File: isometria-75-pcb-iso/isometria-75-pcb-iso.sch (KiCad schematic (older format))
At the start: 32 parts, among them J101 USB, J102 SPI, J103 Conn_01x01_Male, Q101 AO3400A, SW101 RST, SW102 BOOT, U101 XC6206P332MR, U102 STM32F072CBTx

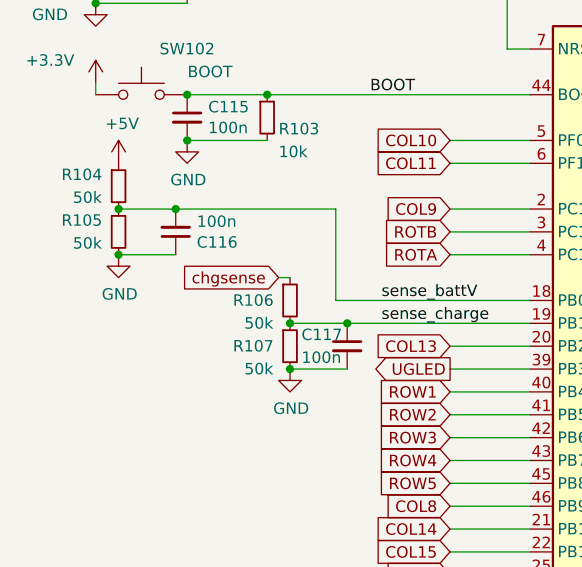
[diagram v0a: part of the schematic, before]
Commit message: final touches
changed some 0603 to 0402 for consistency, added vias to properly better ground planes, added LCSC part numbers for jlcpcb assembly
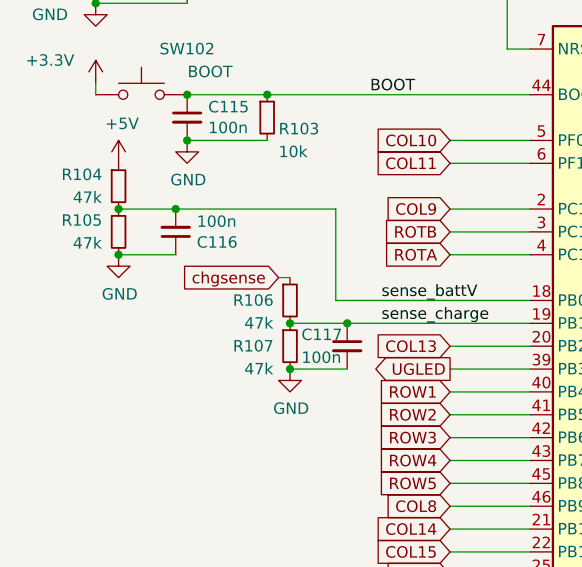
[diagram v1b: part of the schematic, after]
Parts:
- C101, C102: LCSC (none) -> C16133
- C103: LCSC (none) -> C7171
- C104, C106: footprint Capacitor_SMD:C_0603_1608Metric -> Capacitor_SMD:C_0402_1005Metric; LCSC (none) -> C52923
- C105, C112: footprint Capacitor_SMD:C_0603_1608Metric -> Capacitor_SMD:C_0402_1005Metric; LCSC (none) -> C23733
- C107, C108, C109, C110, C113, C114, C115, C116, C117: LCSC (none) -> C1525
- C111: LCSC (none) -> C23733
- J101, J102, J103: LCSC (none) -> /
- Q101: LCSC (none) -> C20917
- R101: LCSC (none) -> C25076
- R102: LCSC (none) -> C25077
- R103: LCSC (none) -> C25744
- R104, R105, R106, R107: value 50k -> 47k; LCSC (none) -> C25792
- SW101, SW102: LCSC (none) -> C318886
- U101: LCSC (none) -> C5446
- U102: LCSC (none) -> C81720
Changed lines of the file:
@@
 F 2 "Package_QFP:LQFP-48_7x7mm_P0.5mm" H 2850 3550 50  0001 R CNN
 F 3 "http://www.st.com/st-web-ui/static/active/en/resource/technical/document/datasheet/DM00090510.pdf" H 3450 4950 50  0001 C CNN
+F 4 "C81720" H 3450 4950 50  0001 C CNN "LCSC"
 	1    3450 4950
 	1    0    0    -1
@@
 F 2 "Capacitor_SMD:C_0402_1005Metric" H 4200 3550 50  0001 C CNN
 F 3 "~" H 4200 3550 50  0001 C CNN
+F 4 "C1525" H 4200 3550 50  0001 C CNN "LCSC"
 	1    4200 3550
 	1    0    0    -1
@@
 F 2 "Capacitor_SMD:C_0402_1005Metric" H 1250 3350 50  0001 C CNN
 F 3 "~" H 1250 3350 50  0001 C CNN
+F 4 "C1525" H 1250 3350 50  0001 C CNN "LCSC"
 	1    1250 3350
 	1    0    0    -1
@@
 F 2 "Resistor_SMD:R_0402_1005Metric" H 3750 3250 50  0001 C CNN
 F 3 "~" H 3750 3250 50  0001 C CNN
+F 4 "C25077" H 3750 3250 50  0001 C CNN "LCSC"
 	1    3750 3250
 	0    -1   -1   0
@@
 F 2 "Package_TO_SOT_SMD:SOT-23" H 4400 1450 50  0001 C CNN
 F 3 "https://datasheet.lcsc.com/szlcsc/Alpha-Omega-Semicon-AOS-AO3400A_C20917.pdf" H 4200 1350 50  0001 C CNN
+F 4 "C20917" H 4200 1350 50  0001 C CNN "LCSC"
 	1    4200 1350
 	1    0    0    -1
@@
 F 2 "Capacitor_SMD:C_0402_1005Metric" H 1950 4950 50  0001 C CNN
 F 3 "~" H 1950 4950 50  0001 C CNN
+F 4 "C1525" H 1950 4950 50  0001 C CNN "LCSC"
 	1    1950 4950
 	1    0    0    -1
@@
 P 1700 4950
 F 0 "R107" H 1450 4950 50  0000 L CNN
-F 1 "50k" H 1500 4850 50  0000 L CNN
+F 1 "47k" H 1500 4850 50  0000 L CNN
 F 2 "Resistor_SMD:R_0402_1005Metric" H 1700 4950 50  0001 C CNN
 F 3 "~" H 1700 4950 50  0001 C CNN
+F 4 "C25792" H 1700 4950 50  0001 C CNN "LCSC"
 	1    1700 4950
 	1    0    0    -1
@@
 P 1700 4750
 F 0 "R106" H 1450 4750 50  0000 L CNN
-F 1 "50k" H 1500 4650 50  0000 L CNN
+F 1 "47k" H 1500 4650 50  0000 L CNN
 F 2 "Resistor_SMD:R_0402_1005Metric" H 1700 4750 50  0001 C CNN
 F 3 "~" H 1700 4750 50  0001 C CNN
+F 4 "C25792" H 1700 4750 50  0001 C CNN "LCSC"
 	1    1700 4750
 	1    0    0    -1
@@
 F 2 "Resistor_SMD:R_0402_1005Metric" H 3900 1350 50  0001 C CNN
 F 3 "~" H 3900 1350 50  0001 C CNN
+F 4 "C25076" H 3900 1350 50  0001 C CNN "LCSC"
 	1    3900 1350
 	0    -1   1    0
@@
 F 2 "Connector_JST:JST_SH_SM05B-SRSS-TB_1x05-1MP_P1.00mm_Horizontal" H 950 1150 50  0001 C CNN
 F 3 "http://www.jst-mfg.com/product/pdf/eng/ePH.pdf" H 950 1150 50  0001 C CNN
+F 4 "/" H 950 1150 50  0001 C CNN "LCSC"
 	1    950  1150
 	-1   0    0    1
@@
 F 0 "C106" H 3292 2496 50  0000 L CNN
 F 1 "1u" H 3292 2405 50  0000 L CNN
-F 2 "Capacitor_SMD:C_0603_1608Metric" H 3200 2450 50  0001 C CNN
+F 2 "Capacitor_SMD:C_0402_1005Metric" H 3200 2450 50  0001 C CNN
 F 3 "~" H 3200 2450 50  0001 C CNN
+F 4 "C52923" H 3200 2450 50  0001 C CNN "LCSC"
 	1    3200 2450
 	1    0    0    -1
@@
 F 0 "C104" H 1942 2496 50  0000 L CNN
 F 1 "1u" H 1942 2405 50  0000 L CNN
-F 2 "Capacitor_SMD:C_0603_1608Metric" H 1850 2450 50  0001 C CNN
+F 2 "Capacitor_SMD:C_0402_1005Metric" H 1850 2450 50  0001 C CNN
 F 3 "~" H 1850 2450 50  0001 C CNN
+F 4 "C52923" H 1850 2450 50  0001 C CNN "LCSC"
 	1    1850 2450
 	1    0    0    -1
@@
 F 2 "Package_TO_SOT_SMD:SOT-23" H 2800 2525 50  0001 C CIN
 F 3 "https://www.torexsemi.com/file/xc6206/XC6206.pdf" H 2800 2300 50  0001 C CNN
+F 4 "C5446" H 2800 2300 50  0001 C CNN "LCSC"
 	1    2800 2300
 	1    0    0    -1
@@
 F 2 "Capacitor_SMD:C_0402_1005Metric" H 5200 2450 50  0001 C CNN
 F 3 "~" H 5200 2450 50  0001 C CNN
+F 4 "C23733" H 5200 2450 50  0001 C CNN "LCSC"
 	1    5200 2450
 	1    0    0    -1
@@
 F 2 "Capacitor_SMD:C_0402_1005Metric" H 4800 2450 50  0001 C CNN
 F 3 "~" H 4800 2450 50  0001 C CNN
+F 4 "C1525" H 4800 2450 50  0001 C CNN "LCSC"
 	1    4800 2450
 	1    0    0    -1
@@
 F 2 "Capacitor_SMD:C_0402_1005Metric" H 4400 2450 50  0001 C CNN
 F 3 "~" H 4400 2450 50  0001 C CNN
+F 4 "C1525" H 4400 2450 50  0001 C CNN "LCSC"
 	1    4400 2450
 	1    0    0    -1
@@
 F 2 "Capacitor_SMD:C_0402_1005Metric" H 4000 2450 50  0001 C CNN
 F 3 "~" H 4000 2450 50  0001 C CNN
+F 4 "C1525" H 4000 2450 50  0001 C CNN "LCSC"
 	1    4000 2450
 	1    0    0    -1
@@
 F 2 "Capacitor_SMD:C_0402_1005Metric" H 3600 2450 50  0001 C CNN
 F 3 "~" H 3600 2450 50  0001 C CNN
+F 4 "C1525" H 3600 2450 50  0001 C CNN "LCSC"
 	1    3600 2450
 	1    0    0    -1
@@
 F 0 "C105" H 2342 2496 50  0000 L CNN
 F 1 "4.7u" H 2342 2405 50  0000 L CNN
-F 2 "Capacitor_SMD:C_0603_1608Metric" H 2250 2450 50  0001 C CNN
+F 2 "Capacitor_SMD:C_0402_1005Metric" H 2250 2450 50  0001 C CNN
 F 3 "~" H 2250 2450 50  0001 C CNN
+F 4 "C23733" H 2250 2450 50  0001 C CNN "LCSC"
 	1    2250 2450
 	1    0    0    -1
@@
 F 0 "C112" H 5692 2496 50  0000 L CNN
 F 1 "4.7u" H 5692 2405 50  0000 L CNN
-F 2 "Capacitor_SMD:C_0603_1608Metric" H 5600 2450 50  0001 C CNN
+F 2 "Capacitor_SMD:C_0402_1005Metric" H 5600 2450 50  0001 C CNN
 F 3 "~" H 5600 2450 50  0001 C CNN
+F 4 "C23733" H 5600 2450 50  0001 C CNN "LCSC"
 	1    5600 2450
 	1    0    0    -1
@@
 F 2 "Capacitor_SMD:C_0402_1005Metric" H 1250 3950 50  0001 C CNN
 F 3 "~" H 1250 3950 50  0001 C CNN
+F 4 "C1525" H 1250 3950 50  0001 C CNN "LCSC"
 	1    1250 3950
 	1    0    0    -1
@@
 F 2 "Resistor_SMD:R_0402_1005Metric" H 1600 3950 50  0001 C CNN
 F 3 "~" H 1600 3950 50  0001 C CNN
+F 4 "C25744" H 1600 3950 50  0001 C CNN "LCSC"
 	1    1600 3950
 	1    0    0    -1
@@
 F 2 "random-keyboard-parts:SKQG-1155865" H 1050 3450 50  0001 C CNN
 F 3 "~" H 1050 3450 50  0001 C CNN
+F 4 "C318886" H 1050 3250 50  0001 C CNN "LCSC"
 	1    1050 3250
 	1    0    0    -1
@@
 F 2 "random-keyboard-parts:SKQG-1155865" H 1050 4050 50  0001 C CNN
 F 3 "~" H 1050 4050 50  0001 C CNN
+F 4 "C318886" H 1050 3850 50  0001 C CNN "LCSC"
 	1    1050 3850
 	1    0    0    -1
@@
 F 2 "Connector_JST:JST_SH_SM08B-SRSS-TB_1x08-1MP_P1.00mm_Horizontal" H 2200 1250 50  0001 C CNN
 F 3 "~" H 2200 1250 50  0001 C CNN
+F 4 "/" H 2200 1250 50  0001 C CNN "LCSC"
 	1    2200 1250
 	-1   0    0    1
@@
 P 950 4250
 F 0 "R104" H 700 4300 50  0000 L CNN
-F 1 "50k" H 750 4200 50  0000 L CNN
+F 1 "47k" H 750 4200 50  0000 L CNN
 F 2 "Resistor_SMD:R_0402_1005Metric" H 950 4250 50  0001 C CNN
 F 3 "~" H 950 4250 50  0001 C CNN
+F 4 "C25792" H 950 4250 50  0001 C CNN "LCSC"
 	1    950  4250
 	1    0    0    -1
@@
 P 950 4450
 F 0 "R105" H 700 4500 50  0000 L CNN
-F 1 "50k" H 750 4400 50  0000 L CNN
+F 1 "47k" H 750 4400 50  0000 L CNN
 F 2 "Resistor_SMD:R_0402_1005Metric" H 950 4450 50  0001 C CNN
 F 3 "~" H 950 4450 50  0001 C CNN
+F 4 "C25792" H 950 4450 50  0001 C CNN "LCSC"
 	1    950  4450
 	1    0    0    -1
@@
 F 2 "Capacitor_SMD:C_0402_1005Metric" H 1200 4450 50  0001 C CNN
 F 3 "~" H 1200 4450 50  0001 C CNN
+F 4 "C1525" H 1200 4450 50  0001 C CNN "LCSC"
 	1    1200 4450
 	1    0    0    1
@@
 F 2 "Capacitor_Tantalum_SMD:CP_EIA-3216-18_Kemet-A" H 1450 2450 50  0001 C CNN
 F 3 "~" H 1450 2450 50  0001 C CNN
+F 4 "C7171" H 1450 2450 50  0001 C CNN "LCSC"
 	1    1450 2450
 	1    0    0    -1
@@
 F 2 "Capacitor_Tantalum_SMD:CP_EIA-3528-21_Kemet-B" H 1050 2450 50  0001 C CNN
 F 3 "~" H 1050 2450 50  0001 C CNN
+F 4 "C16133" H 1050 2450 50  0001 C CNN "LCSC"
 	1    1050 2450
 	1    0    0    -1
@@
 F 2 "Capacitor_Tantalum_SMD:CP_EIA-3528-21_Kemet-B" H 650 2450 50  0001 C CNN
 F 3 "~" H 650 2450 50  0001 C CNN
+F 4 "C16133" H 650 2450 50  0001 C CNN "LCSC"
 	1    650  2450
 	1    0    0    -1
@@
 F 2 "Connector_PinHeader_2.54mm:PinHeader_1x01_P2.54mm_Vertical" H 4700 4850 50  0001 C CNN
 F 3 "~" H 4700 4850 50  0001 C CNN
+F 4 "/" H 4700 4850 50  0001 C CNN "LCSC"
 	1    4700 4850
 	-1   0    0    1
